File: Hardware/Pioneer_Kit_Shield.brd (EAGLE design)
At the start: 53.3 x 59.7 mm, 42 parts, among them J1 AMP FCI 10103594-0001LF, U1 USD-SOCKETNEW, U2 ARDUINO_UNO_R3_SHIELDUNO_R3_S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, U3 74HC4050, U4 PCA9306, U5 TPS62065

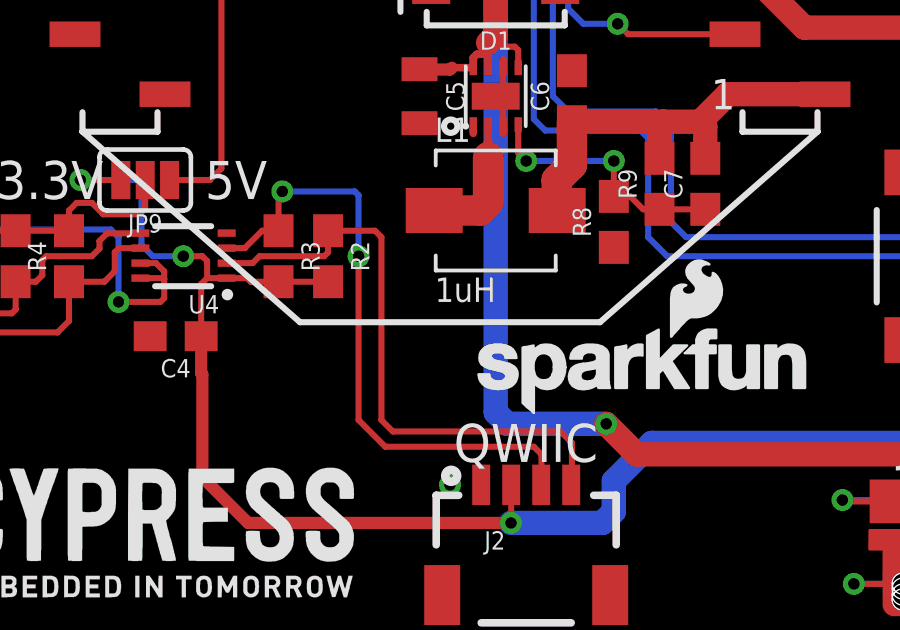
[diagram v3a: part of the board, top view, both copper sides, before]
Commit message: Added testpoints
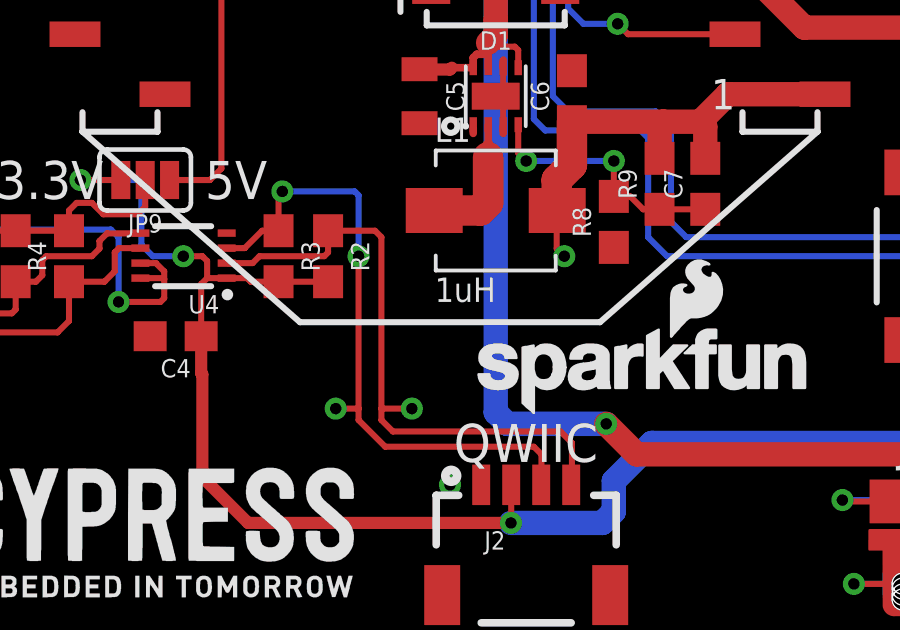
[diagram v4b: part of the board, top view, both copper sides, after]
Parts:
- added TP1, TP2, TP3: TEST-POINTTP_15TH_THRU, SparkFun-Connectors:TP_15TH
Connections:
- removed net N$5: J2.3, R3.1, U4.3
- removed net N$8: J2.4, R2.1, U4.2
- new net SCL_2: J2.4, R2.1, TP1.P$1, U4.2
- new net SDA_2: J2.3, R3.1, TP2.P$1, U4.3
- net VCC: now also TP3.P$1
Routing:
- net SDA_2: track 0.00 -> 21.8 mm, vias 0 -> 2
- net SCL_2: track 0.00 -> 21.3 mm
- net N$5: track 21.0 -> 0.00 mm, vias 2 -> 0
- net N$8: track 20.3 -> 0.00 mm
- net VCC: track 14.6 -> 16.2 mm
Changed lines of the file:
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@@
 <layers>
 <layer number="1" name="Top" color="4" fill="1" visible="yes" active="yes"/>
-<layer number="2" name="Route2" color="1" fill="3" visible="yes" active="yes"/>
-<layer number="15" name="Route15" color="4" fill="6" visible="yes" active="yes"/>
+<layer number="2" name="Route2" color="1" fill="3" visible="no" active="yes"/>
+<layer number="15" name="Route15" color="4" fill="6" visible="no" active="yes"/>
 <layer number="16" name="Bottom" color="1" fill="1" visible="yes" active="yes"/>
 <layer number="17" name="Pads" color="2" fill="1" visible="yes" active="yes"/>
@@
 <layer number="23" name="tOrigins" color="15" fill="1" visible="yes" active="yes"/>
 <layer number="24" name="bOrigins" color="15" fill="1" visible="yes" active="yes"/>
-<layer number="25" name="tNames" color="7" fill="1" visible="yes" active="yes"/>
-<layer number="26" name="bNames" color="7" fill="1" visible="yes" active="yes"/>
-<layer number="27" name="tValues" color="7" fill="1" visible="yes" active="yes"/>
-<layer number="28" name="bValues" color="7" fill="1" visible="yes" active="yes"/>
-<layer number="29" name="tStop" color="7" fill="3" visible="yes" active="yes"/>
-<layer number="30" name="bStop" color="7" fill="6" visible="yes" active="yes"/>
-<layer number="31" name="tCream" color="7" fill="4" visible="yes" active="yes"/>
-<layer number="32" name="bCream" color="7" fill="5" visible="yes" active="yes"/>
-<layer number="39" name="tKeepout" color="4" fill="11" visible="yes" active="yes"/>
-<layer number="40" name="bKeepout" color="1" fill="11" visible="yes" active="yes"/>
-<layer number="41" name="tRestrict" color="4" fill="10" visible="yes" active="yes"/>
-<layer number="42" name="bRestrict" color="1" fill="10" visible="yes" active="yes"/>
-<layer number="43" name="vRestrict" color="2" fill="10" visible="yes" active="yes"/>
-<layer number="44" name="Drills" color="7" fill="1" visible="yes" active="yes"/>
+<layer number="25" name="tNames" color="7" fill="1" visible="no" active="yes"/>
+<layer number="26" name="bNames" color="7" fill="1" visible="no" active="yes"/>
+<layer number="27" name="tValues" color="7" fill="1" visible="no" active="yes"/>
+<layer number="28" name="bValues" color="7" fill="1" visible="no" active="yes"/>
+<layer number="29" name="tStop" color="7" fill="3" visible="no" active="yes"/>
+<layer number="30" name="bStop" color="7" fill="6" visible="no" active="yes"/>
+<layer number="31" name="tCream" color="7" fill="4" visible="no" active="yes"/>
+<layer number="32" name="bCream" color="7" fill="5" visible="no" active="yes"/>
+<layer number="39" name="tKeepout" color="4" fill="11" visible="no" active="yes"/>
+<layer number="40" name="bKeepout" color="1" fill="11" visible="no" active="yes"/>
+<layer number="41" name="tRestrict" color="4" fill="10" visible="no" active="yes"/>
+<layer number="42" name="bRestrict" color="1" fill="10" visible="no" active="yes"/>
+<layer number="43" name="vRestrict" color="2" fill="10" visible="no" active="yes"/>
+<layer number="44" name="Drills" color="7" fill="1" visible="no" active="yes"/>
 <layer number="45" name="Holes" color="7" fill="1" visible="yes" active="yes"/>
-<layer number="46" name="Milling" color="3" fill="1" visible="yes" active="yes"/>
-<layer number="47" name="Measures" color="7" fill="1" visible="yes" active="yes"/>
-<layer number="48" name="Document" color="7" fill="1" visible="yes" active="yes"/>
-<layer number="49" name="Reference" color="7" fill="1" visible="yes" active="yes"/>
+<layer number="46" name="Milling" color="3" fill="1" visible="no" active="yes"/>
+<layer number="47" name="Measures" color="7" fill="1" visible="no" active="yes"/>
+<layer number="48" name="Document" color="7" fill="1" visible="no" active="yes"/>
+<layer number="49" name="Reference" color="7" fill="1" visible="no" active="yes"/>
 <layer number="51" name="tDocu" color="6" fill="1" visible="yes" active="yes"/>
-<layer number="52" name="bDocu" color="7" fill="1" visible="yes" active="yes"/>
+<layer number="52" name="bDocu" color="7" fill="1" visible="no" active="yes"/>
 <layer number="3" name="Route3" color="4" fill="3" visible="no" active="no"/>
 <layer number="4" name="Route4" color="1" fill="4" visible="no" active="no"/>
@@
 <attribute name="PROD_ID" value="RES-13247" x="33.655" y="15.113" size="1.778" layer="27" font="vector" ratio="15" rot="R90" display="off"/>
 </element>
+<element name="TP1" library="SparkFun-Connectors" package="TP_15TH" value="TEST-POINTTP_15TH_THRU" x="25.4" y="7.62"/>
+<element name="TP2" library="SparkFun-Connectors" package="TP_15TH" value="TEST-POINTTP_15TH_THRU" x="22.86" y="7.62"/>
+<element name="TP3" library="SparkFun-Connectors" package="TP_15TH" value="TEST-POINTTP_15TH_THRU" x="30.48" y="12.7"/>
 </elements>
 <signals>
@@
 <wire x1="39.17" y1="22.1" x2="39.17" y2="22.806" width="0.2032" layer="1"/>
 </signal>
-<signal name="N$5">
+<signal name="SDA_2">
 <contactref element="J2" pad="3"/>
 <contactref element="U4" pad="3"/>
@@
 <wire x1="23.622" y1="14.732" x2="23.622" y2="12.7" width="0.2032" layer="16"/>
 <via x="23.622" y="12.7" extent="1-16" drill="0.381"/>
-<wire x1="23.622" y1="12.7" x2="23.622" y2="7.239" width="0.2032" layer="1"/>
+<wire x1="23.622" y1="12.7" x2="23.622" y2="7.62" width="0.2032" layer="1"/>
+<wire x1="23.622" y1="7.62" x2="23.622" y2="7.239" width="0.2032" layer="1"/>
 <wire x1="23.622" y1="7.239" x2="24.511" y2="6.35" width="0.2032" layer="1"/>
 <wire x1="24.511" y1="6.35" x2="29.464" y2="6.35" width="0.2032" layer="1"/>
@@
 <wire x1="29.718" y1="6.096" x2="29.718" y2="5.088" width="0.2032" layer="1"/>
 <wire x1="29.718" y1="5.088" x2="29.71" y2="5.08" width="0.2032" layer="1"/>
+<contactref element="TP2" pad="P$1"/>
+<wire x1="22.86" y1="7.62" x2="23.622" y2="7.62" width="0.2032" layer="1"/>
 </signal>
-<signal name="N$8">
+<signal name="SCL_2">
 <contactref element="J2" pad="4"/>
 <contactref element="U4" pad="2"/>
@@
 <wire x1="22.606" y1="13.55" x2="24.169" y2="13.55" width="0.2032" layer="1"/>
 <wire x1="24.169" y1="13.55" x2="24.384" y2="13.335" width="0.2032" layer="1"/>
-<wire x1="24.384" y1="13.335" x2="24.384" y2="7.239" width="0.2032" layer="1"/>
+<wire x1="24.384" y1="13.335" x2="24.384" y2="7.62" width="0.2032" layer="1"/>
+<wire x1="24.384" y1="7.62" x2="24.384" y2="7.239" width="0.2032" layer="1"/>
 <wire x1="24.384" y1="7.239" x2="24.765" y2="6.858" width="0.2032" layer="1"/>
 <wire x1="24.765" y1="6.858" x2="30.353" y2="6.858" width="0.2032" layer="1"/>
@@
 <wire x1="22.479" y1="12.7" x2="22.606" y2="12.827" width="0.2032" layer="1"/>
 <wire x1="22.606" y1="12.827" x2="22.606" y2="13.55" width="0.2032" layer="1"/>
+<contactref element="TP1" pad="P$1"/>
+<wire x1="25.4" y1="7.62" x2="24.384" y2="7.62" width="0.2032" layer="1"/>
 </signal>
 <signal name="N$9">
@@
 <wire x1="39.17" y1="18.1" x2="35.929" y2="18.1" width="0.8128" layer="1"/>
 <wire x1="35.929" y1="18.1" x2="35.013" y2="17.184" width="0.8128" layer="1"/>
+<contactref element="TP3" pad="P$1"/>
+<wire x1="30.226" y1="14.242" x2="30.226" y2="12.954" width="0.2032" layer="1"/>
+<wire x1="30.226" y1="12.954" x2="30.48" y2="12.7" width="0.2032" layer="1"/>
 </signal>
 <signal name="!CD">
